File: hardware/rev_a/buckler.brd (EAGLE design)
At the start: 160 x 100 mm, 19 parts, among them J1 ARDUINO_R3_SHIELD_ICSP_NRF528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, J2 DM3AT-SF-PEJM5, U11 SI7021-A20-GM1, U12 SIP32510, U14 MPU-9250, U8 MAX44009, U9 MS5637-02BA03

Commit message: Checkpoint. Done with schematic
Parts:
- added A1: NHD-0216KZWSERIAL, headers:NHD-0216KZW
- added C1, C2, C3, C4: 0.1uF, passives:0402_CAP
- added D1: (no value), passives:SOD923
- added D2: RED, leds:LED-0603
- added D3: GREEN, leds:LED-0603
- added D4: BLUE, leds:LED-0603
- added D5: YELLOW, leds:LED-0603
- added J3: DB25_5747846, headers:DB25_5747846
- added J4, J5, J6, J7, J8, J9: 4P-2.0, headers:HW4-2.0
- added R10, R11, R2, R3, R4: 10k, passives:0402_RES
- added R5, R6, R7, R8: 1k, passives:0402_RES
- added S1, S3, S7: PTS645SM43SMTR92, switches:PTS645
- added S2: B3U-1000P, switches:B3U-1000P
- added S25, S4: TE_SSA12/SPDT, switches:TE_SSA12/SPDT
- added TP1, TP2, TP27, TP28, TP3, TP4, TP5: TEST_POINT_0.040IN, headers:TESTPOINT_0.040IN
- added U1: ADXL327, chips:LFCSP-16
- J1: value ARDUINO_R3_SHIELD_ICSP_NRF52840DK -> NRF52840DK_SHIELD; device headers:ARDUINO_R3_SHIELD_ICSP_NRF52840DK -> headers:NRF52840DK_SHIELD
- moved J1 4.02 mm to (15.2, 62.2)
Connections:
- removed net !IMU_INT: R1.1, U14.12
- removed net !LT_INT: R9.1, U8.4
- removed net N$34: U9.3
- removed net N$41: U9.2
- removed net N$50: U11.6
- removed net N$51: U8.6
- removed net N$52: U8.5
- new net !BUTTON_0: J1.P1.12, R10.1, S1.1, S1.2
- new net !BUTTON_1: J1.P1.13, R11.1, S3.1, S3.2
- new net !IMU_INTERRUPT: J1.P1.01, R1.1, TP5.TESTPOINT, U14.12
- new net !LCD_CS: A1.16, J1.P1.03
- new net !LED_0: D2.C, J1.P1.06
- new net !LED_1: D3.C, J1.P1.07
- new net !LED_2: D4.C, J1.P1.10
- new net !LED_3: D5.C, J1.P1.11
- new net !LIGHT_INTERRUPT: J1.P1.02, R9.1, TP4.TESTPOINT, U8.4
- new net ANALOG_ACCEL_X: C4.1, J1.P0.29, TP28.TESTPOINT, U1.12
- new net ANALOG_ACCEL_Y: C3.1, J1.P0.30, TP27.TESTPOINT, U1.10
- new net ANALOG_ACCEL_Z: C2.1, J1.P0.31, TP1.TESTPOINT, U1.8
- new net EXTERN_RX: J1.P0.25, J3.1, J5.2
- new net EXTERN_TX: J1.P0.24, J3.2, J5.1
- new net GROVE_A0: J1.P0.02, J6.1
- new net GROVE_A1: J1.P0.03, J6.2
- new net GROVE_A2: J1.P0.28, J7.1
- new net GROVE_D0: J1.P0.04, J8.1
- new net GROVE_D1: J1.P1.08, J8.2
- new net GROVE_D2: J1.P1.09, J9.1
- new net LCD_MISO: A1.13, J1.P0.14
- new net LCD_MOSI: A1.14, J1.P0.16
- new net LCD_SCLK: A1.12, J1.P0.12
- new net N$2: D1.P$2, J3.8, J3.9
- new net N$25: D2.A, R5.2
- new net N$3: D3.A, R6.2
- new net N$4: D4.A, R7.2
- new net N$5: D5.A, R8.2
- new net N$7: S2.1, U1.2
- new net SWITCH_0: J1.P1.14, S25.IN
- new net SWITCH_1: J1.P1.15, S4.IN
- net !SD_CS: now also J1.P1.04
- net !SD_DETECT: now also J1.P1.05
- net +3V3: now also A1.2, C1.1, J1.3.3V@0, J1.3.3V@1, J1.3.3V@2, J4.3, J5.3, J6.3, J7.3, J8.3, J9.3, R10.2, R11.2, R2.2, R3.2, R4.2, R5.1, R6.1, R7.1, R8.1, S2.2, S25.2, S4.2, U1.14, U1.15; no longer J1.3.3V, J1.IOREF
- net +5V: now also D1.P$1; no longer J1.5V_ICSP
- net GND: now also A1.1, C1.2, C2.2, C3.2, C4.2, J1.GND@3, J3.16, J3.20, J3.21, J3.24, J3.25, J3.6, J4.4, J5.4, J6.4, J7.4, J8.4, J9.4, S1.3, S1.4, S25.1, S3.3, S3.4, S4.1, S7.3, S7.4, U1.3, U1.5, U1.6, U1.7; no longer J1.GND_ICSP
- net N$1: now also J1.P0.18, R2.1, S7.1, S7.2; no longer U11.1
- net SD_MISO: now also J1.P0.13
- net SD_MOSI: now also J1.P0.15
- net SD_SCLK: now also J1.P0.11
- net SENSORS_SCL: now also J1.P0.27, J4.1, R3.1, TP3.TESTPOINT, U11.6, U8.5, U9.3
- net SENSORS_SDA: now also J1.P0.26, J4.2, R4.1, TP2.TESTPOINT, U11.1, U8.6, U9.2

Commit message: Checkpoint. 50 airwares remaining!
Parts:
- removed TP1, TP2, TP27, TP28, TP3: TEST_POINT_0.040IN, headers:TESTPOINT_0.040IN
- added TP10, TP11, TP12, TP13, TP14, TP15, TP16, TP17, TP18, TP19, TP20, TP21, TP22, TP23, TP24, TP25, TP26, TP29, TP30, TP31, TP32, TP33, TP34, TP35, TP36, TP37, TP38, TP39, TP40, TP41, TP42, TP43, TP44, TP6, TP7, TP8, TP9: TEST_POINT_0.040IN, headers:TESTPOINT_0.040IN
- moved J9 375.4 mm to (55.9, 10.2), turned to 90 degrees
- moved J8 351.2 mm to (25.4, 10.2), turned to 90 degrees
- moved J7 343.7 mm to (35.6, 10.2), turned to 90 degrees
- moved R4 337.1 mm to (54.0, 103.5), turned to 180 degrees
- moved J6 336.9 mm to (45.7, 10.2), turned to 90 degrees
- moved R3 334.9 mm to (56.5, 103.5)
- moved S7 319.3 mm to (6.35, 114.3)
- moved R2 318.5 mm to (13.3, 117.5), turned to 90 degrees
- moved S25 313.7 mm to (21.6, 30.5)
- moved S4 313.7 mm to (21.6, 21.6)
- moved J5 308.2 mm to (5.08, 10.2), turned to 90 degrees
- moved R11 303.7 mm to (14.6, 27.3)
- moved J4 300.6 mm to (15.2, 10.2), turned to 90 degrees
- moved R10 294.9 mm to (14.6, 30.5)
- moved S3 291.3 mm to (7.62, 22.9)
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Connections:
- net !BUTTON_0: now also TP36.TESTPOINT
- net !BUTTON_1: now also TP37.TESTPOINT
- net !IMU_INTERRUPT: now also TP6.TESTPOINT; no longer TP5.TESTPOINT
- net !LCD_CS: now also TP8.TESTPOINT
- net !LED_0: now also TP11.TESTPOINT
- net !LED_1: now also TP12.TESTPOINT
- net !LED_2: now also TP13.TESTPOINT
- net !LED_3: now also TP35.TESTPOINT
- net !LIGHT_INTERRUPT: now also TP7.TESTPOINT; no longer TP4.TESTPOINT
- net !SD_CS: now also TP9.TESTPOINT
- net !SD_DETECT: now also TP10.TESTPOINT
- net +3V3: now also TP4.TESTPOINT, TP40.TESTPOINT, TP5.TESTPOINT
- net +5V: now also TP41.TESTPOINT
- net ANALOG_ACCEL_X: now also TP17.TESTPOINT; no longer TP28.TESTPOINT
- net ANALOG_ACCEL_Y: now also TP18.TESTPOINT; no longer TP27.TESTPOINT
- net ANALOG_ACCEL_Z: now also TP19.TESTPOINT; no longer TP1.TESTPOINT
- net EXTERN_RX: now also TP32.TESTPOINT
- net EXTERN_TX: now also TP33.TESTPOINT
- net GND: now also TP42.TESTPOINT, TP43.TESTPOINT, TP44.TESTPOINT
- net GROVE_A0: now also TP14.TESTPOINT
- net GROVE_A1: now also TP15.TESTPOINT
- net GROVE_A2: now also TP16.TESTPOINT
- net GROVE_D0: now also TP34.TESTPOINT
- net GROVE_D1: now also TP29.TESTPOINT
- net GROVE_D2: now also TP26.TESTPOINT
- net LCD_MISO: now also TP22.TESTPOINT
- net LCD_MOSI: now also TP20.TESTPOINT
- net LCD_SCLK: now also TP24.TESTPOINT
- net SD_MISO: now also TP23.TESTPOINT
- net SD_MOSI: now also TP21.TESTPOINT
- net SD_SCLK: now also TP25.TESTPOINT
- net SENSORS_SCL: now also TP30.TESTPOINT; no longer TP3.TESTPOINT
- net SENSORS_SDA: now also TP31.TESTPOINT; no longer TP2.TESTPOINT
- net SWITCH_0: now also TP38.TESTPOINT
- net SWITCH_1: now also TP39.TESTPOINT
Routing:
- net N$1: track 0.00 -> 125.3 mm
- net EXTERN_RX: track 0.00 -> 99.0 mm, vias 0 -> 1
- net EXTERN_TX: track 0.00 -> 95.7 mm
- net GROVE_A1: track 0.00 -> 93.4 mm, vias 0 -> 1
- net GROVE_A2: track 0.00 -> 82.4 mm
- net GND: track 0.00 -> 79.2 mm, vias 0 -> 12
- net GROVE_D0: track 0.00 -> 72.0 mm
- net GROVE_D2: track 0.00 -> 67.1 mm, vias 0 -> 2
- net GROVE_A0: track 0.00 -> 36.4 mm, vias 0 -> 2
- net N$2: track 0.00 -> 35.4 mm, vias 0 -> 1
- net ANALOG_ACCEL_Y: track 0.00 -> 34.2 mm, vias 0 -> 1
- net ANALOG_ACCEL_Z: track 0.00 -> 33.5 mm, vias 0 -> 1
- net ANALOG_ACCEL_X: track 0.00 -> 33.3 mm, vias 0 -> 1
- net !BUTTON_1: track 0.00 -> 32.4 mm, vias 0 -> 2
- net GROVE_D1: track 0.00 -> 31.9 mm, vias 0 -> 1
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- added copper zone on layer 1, net +3V3
- added copper zone on layer 16, net GND
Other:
- board size 160 x 100 mm -> 63.5 x 125.7 mm

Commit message: Routing complete!!
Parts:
- added C13: 10nF, passives:0402_CAP
- added C5: 100nF, passives:0402_CAP
- moved R8 89.0 mm to (55.9, 116.2), turned to 180 degrees
- moved D3 86.0 mm to (52.7, 116.2), turned to 90 degrees
- moved D1 47.7 mm to (16.5, 81.3)
- moved R17 13.9 mm to (29.8, 95.9), turned to 0 degrees
- moved R1 13.6 mm to (27.3, 73.7), turned to 180 degrees
- moved U14 12.1 mm to (31.8, 76.2), turned to 270 degrees
- moved C18 10.6 mm to (27.3, 75.6), turned to 180 degrees
- moved R12 10.5 mm to (20.3, 101.6)
- moved C26 6.63 mm to (23.1, 103.0), turned to 0 degrees
- moved U12 5.46 mm to (26.0, 95.9), turned to 180 degrees
- moved R14 4.62 mm to (22.2, 106.7), turned to 0 degrees
- moved R16 4.49 mm to (22.2, 108.6), turned to 0 degrees
- moved R13 2.69 mm to (29.8, 99.7), turned to 180 degrees
- moved D5 2.54 mm to (6.35, 43.8)
- moved D4 2.54 mm to (8.89, 43.8)
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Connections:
- removed net !LED_3: D5.C, J1.P1.11, TP35.TESTPOINT
- net !LED_1: now also D5.C; no longer D3.C
- net +3V3: now also C13.1, C5.1
- net GND: now also C13.2, C5.2, D3.C
- net N$3: now also R8.2; no longer R6.2
- net N$5: now also R6.2; no longer R8.2
- net SD_ENABLE: now also J1.P1.11, TP35.TESTPOINT
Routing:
- net SENSORS_SCL: track 24.5 -> 142.7 mm, vias 3 -> 8
- net SENSORS_SDA: track 30.9 -> 142.4 mm, vias 0 -> 1
- net SD_MISO: track 13.4 -> 123.2 mm, vias 0 -> 3
- net SD_SCLK: track 9.83 -> 119.0 mm, vias 0 -> 3
- net SD_MOSI: track 17.0 -> 117.2 mm, vias 0 -> 2
- net !BUTTON_0: track 21.1 -> 104.0 mm, vias 0 -> 4
- net !SD_DETECT: track 5.71 -> 86.0 mm, vias 0 -> 2
- net !BUTTON_1: track 32.4 -> 111.2 mm, vias 2 -> 6
- net GROVE_A0: track 36.4 -> 113.4 mm
- net SWITCH_1: track 20.9 -> 97.0 mm, vias 0 -> 4
- net !LED_2: track 9.30 -> 85.4 mm, vias 0 -> 4
- net SWITCH_0: track 11.7 -> 87.2 mm, vias 0 -> 4
- net !SD_CS: track 5.71 -> 74.5 mm, vias 0 -> 4
- net LCD_SCLK: track 9.83 -> 70.3 mm, vias 0 -> 1
- net !LED_1: track 14.2 -> 72.7 mm, vias 0 -> 5
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
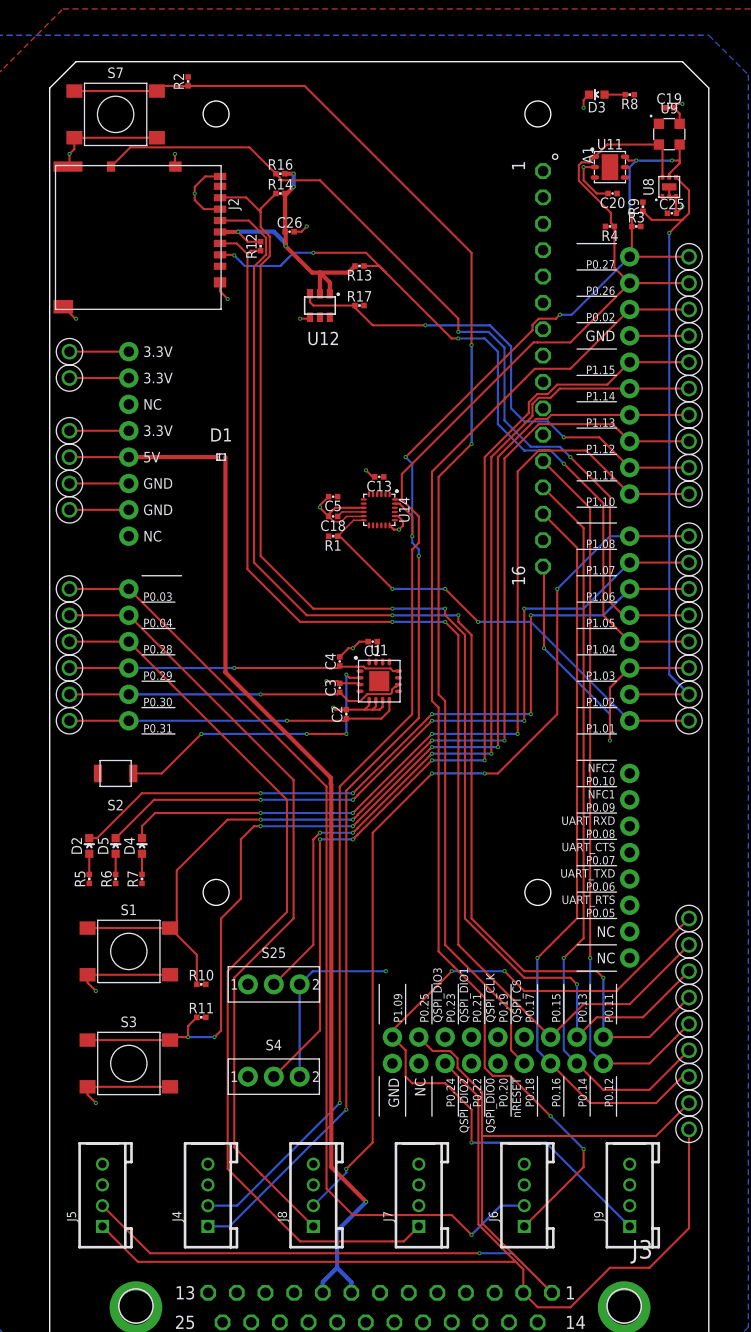
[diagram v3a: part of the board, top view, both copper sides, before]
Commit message: Renumber script, plus some manual tweaks
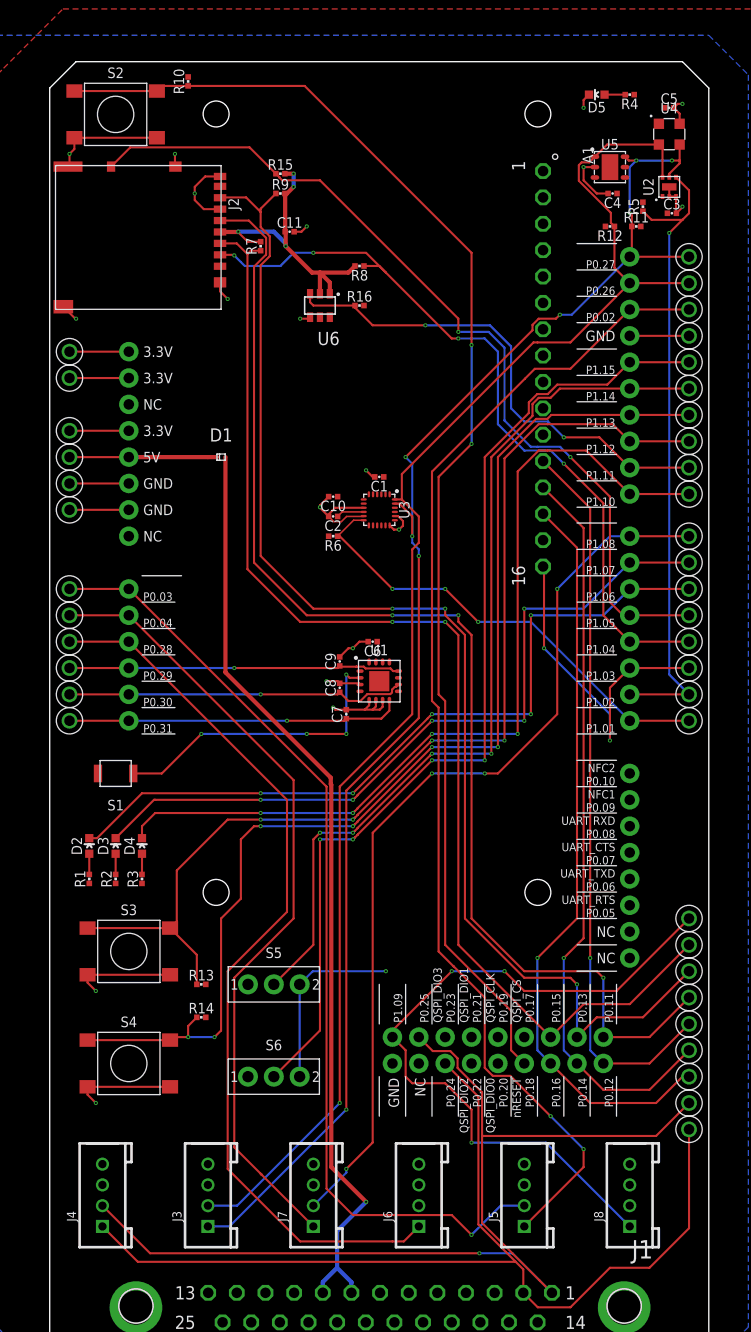
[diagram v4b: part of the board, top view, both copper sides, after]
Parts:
- removed C13: 10nF, passives:0402_CAP
- removed C18: 100nF, passives:0402_CAP
- removed C19, C20: 0.1uF, passives:0402_CAP
- removed C25: 1uF, passives:0402_CAP
- removed R17: 100k, passives:0402_RES
- removed S7: PTS645SM43SMTR92, switches:PTS645
- removed TP40, TP41, TP42, TP43, TP44: TEST_POINT_0.040IN, headers:TESTPOINT_0.040IN
- added C10, C6, C7, C8, C9: 100nF, passives:0402_CAP
- added R15: 100k, passives:0402_RES
- added S6: TE_SSA12/SPDT, switches:TE_SSA12/SPDT
- added TP1, TP2, TP27, TP28, TP3: TEST_POINT_0.040IN, headers:TESTPOINT_0.040IN
- C1: value 0.1uF -> 10nF
- C2, C3, C4: value 0.1uF -> 100nF
- D3: value GREEN -> YELLOW
- D5: value YELLOW -> GREEN
- J1: value NRF52840DK_SHIELD -> DB25_5747846; device headers:NRF52840DK_SHIELD -> headers:DB25_5747846
- J3: value DB25_5747846 -> 4P-2.0; device headers:DB25_5747846 -> headers:HW4-2.0
- J9: value 4P-2.0 -> NRF52840DK_SHIELD; device headers:HW4-2.0 -> headers:NRF52840DK_SHIELD
- R1, R2, R3, R4: value 10k -> 1k
- R5, R6, R7, R8: value 1k -> 10k
- S1: value PTS645SM43SMTR92 -> B3U-1000P; device switches:PTS645 -> switches:B3U-1000P
- S2: value B3U-1000P -> PTS645SM43SMTR92; device switches:B3U-1000P -> switches:PTS645
- S4: value TE_SSA12/SPDT -> PTS645SM43SMTR92; device switches:TE_SSA12/SPDT -> switches:PTS645
- moved J1 99.4 mm to (48.4, 0.76), turned to 180 degrees
- moved TP33 95.8 mm to (1.91, 91.4)
- moved J9 94.5 mm to (7.62, 91.4), turned to 0 degrees
- moved R10 87.0 mm to (13.3, 117.5), turned to 90 degrees
- moved R11 87.0 mm to (56.5, 103.5)
- moved D3 86.0 mm to (6.35, 43.8), turned to 0 degrees
- moved D5 86.0 mm to (52.7, 116.2), turned to 90 degrees
- moved R5 83.9 mm to (57.1, 105.4)
- moved R14 79.7 mm to (14.6, 27.3)
- moved R3 78.9 mm to (8.89, 40.6), turned to 90 degrees
- moved R2 77.2 mm to (6.35, 40.6)
- moved TP15 76.0 mm to (61.6, 21.6)
- moved TP14 71.6 mm to (1.91, 55.9)
- moved TP32 71.4 mm to (61.6, 90.4)
- moved TP24 71.4 mm to (61.6, 98.0)
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- renumbered C26 to C11, S25 to S5, U11 to U5, U12 to U6, U14 to U3, U8 to U2, U9 to U4
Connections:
- net !BUTTON_0: now also J9.P1.12, R13.1, S3.1, S3.2, TP29.TESTPOINT; no longer J1.P1.12, R10.1, S1.1, S1.2, TP36.TESTPOINT
- net !BUTTON_1: now also J9.P1.13, R14.1, S4.1, S4.2, TP30.TESTPOINT; no longer J1.P1.13, R11.1, S3.1, S3.2, TP37.TESTPOINT
- net !IMU_INTERRUPT: now also J9.P1.01, R6.1, TP1.TESTPOINT; no longer J1.P1.01, R1.1, TP6.TESTPOINT
- net !LCD_CS: now also J9.P1.03, TP3.TESTPOINT; no longer J1.P1.03, TP8.TESTPOINT
- net !LED_0: now also J9.P1.06, TP6.TESTPOINT; no longer J1.P1.06, TP11.TESTPOINT
- net !LED_1: now also D3.C, J9.P1.07, TP7.TESTPOINT; no longer D5.C, J1.P1.07, TP12.TESTPOINT
- net !LED_2: now also J9.P1.10, TP8.TESTPOINT; no longer J1.P1.10, TP13.TESTPOINT
- net !LIGHT_INTERRUPT: now also J9.P1.02, R5.1, TP2.TESTPOINT; no longer J1.P1.02, R9.1, TP7.TESTPOINT
- net !SD_CS: now also J9.P1.04, R8.1, TP4.TESTPOINT; no longer J1.P1.04, R13.1, TP9.TESTPOINT
- net !SD_DETECT: now also J9.P1.05, R15.1, TP5.TESTPOINT; no longer J1.P1.05, R16.1, TP10.TESTPOINT
- net +3V3: now also C10.1, C3.1, C4.1, C6.1, J3.3, J9.3.3V@0, J9.3.3V@1, J9.3.3V@2, R1.1, R12.2, R13.2, R14.2, R16.2, R2.1, R3.1, R4.1, R5.2, R6.2, S1.2, S6.2, TP33.TESTPOINT, TP34.TESTPOINT, TP35.TESTPOINT; no longer C13.1, C19.1, C20.1, C25.1, J1.3.3V@0, J1.3.3V@1, J1.3.3V@2, J9.3, R1.2, R17.2, R2.2, R3.2, R4.2, R5.1, R6.1, R7.1, R8.1, R9.2, S2.2, S4.2, TP4.TESTPOINT, TP40.TESTPOINT, TP5.TESTPOINT
- net +5V: now also J9.5V, TP36.TESTPOINT; no longer J1.5V, TP41.TESTPOINT
- net ANALOG_ACCEL_X: now also C9.1, J9.P0.29, TP12.TESTPOINT; no longer C4.1, J1.P0.29, TP17.TESTPOINT
- net ANALOG_ACCEL_Y: now also C8.1, J9.P0.30, TP13.TESTPOINT; no longer C3.1, J1.P0.30, TP18.TESTPOINT
- net ANALOG_ACCEL_Z: now also C7.1, J9.P0.31, TP14.TESTPOINT; no longer C2.1, J1.P0.31, TP19.TESTPOINT
- net EXTERN_RX: now also J1.1, J4.2, J9.P0.25, TP25.TESTPOINT; no longer J1.P0.25, J3.1, J5.2, TP32.TESTPOINT
- net EXTERN_TX: now also J1.2, J4.1, J9.P0.24, TP26.TESTPOINT; no longer J1.P0.24, J3.2, J5.1, TP33.TESTPOINT
- net GND: now also C10.2, C6.2, C7.2, C8.2, C9.2, D5.C, J1.16, J1.20, J1.21, J1.24, J1.25, J1.6, J3.4, J9.GND@0, J9.GND@1, J9.GND@2, J9.GND@3, S2.3, S2.4, S4.3, S4.4, S6.1, TP37.TESTPOINT, TP38.TESTPOINT, TP39.TESTPOINT; no longer C13.2, C18.2, C19.2, C20.2, C25.2, D3.C, J1.GND@0, J1.GND@1, J1.GND@2, J1.GND@3, J3.16, J3.20, J3.21, J3.24, J3.25, J3.6, J9.4, S1.3, S1.4, S4.1, S7.3, S7.4, TP42.TESTPOINT, TP43.TESTPOINT, TP44.TESTPOINT
- net GROVE_A0: now also J5.1, J9.P0.02, TP9.TESTPOINT; no longer J1.P0.02, J6.1, TP14.TESTPOINT
- net GROVE_A1: now also J5.2, J9.P0.03, TP10.TESTPOINT; no longer J1.P0.03, J6.2, TP15.TESTPOINT
- net GROVE_A2: now also J6.1, J9.P0.28, TP11.TESTPOINT; no longer J1.P0.28, J7.1, TP16.TESTPOINT
- net GROVE_D0: now also J7.1, J9.P0.04, TP27.TESTPOINT; no longer J1.P0.04, J8.1, TP34.TESTPOINT
- net GROVE_D1: now also J7.2, J9.P1.08, TP22.TESTPOINT; no longer J1.P1.08, J8.2, TP29.TESTPOINT
- net GROVE_D2: now also J8.1, J9.P1.09, TP21.TESTPOINT; no longer J1.P1.09, J9.1, TP26.TESTPOINT
- net LCD_MISO: now also J9.P0.14, TP17.TESTPOINT; no longer J1.P0.14, TP22.TESTPOINT
- net LCD_MOSI: now also J9.P0.16, TP15.TESTPOINT; no longer J1.P0.16, TP20.TESTPOINT
- net LCD_SCLK: now also J9.P0.12, TP19.TESTPOINT; no longer J1.P0.12, TP24.TESTPOINT
- net N$1: now also J9.P0.18, R10.1, S2.1, S2.2; no longer J1.P0.18, R2.1, S7.1, S7.2
- net N$18: now also R15.2, R7.2, R8.2, R9.2; no longer R12.2, R13.2, R14.2, R16.2
- net N$19: now also C2.1; no longer C18.1
- net N$2: now also J1.8, J1.9; no longer J3.8, J3.9
- net N$25: now also R1.2; no longer R5.2
- net N$3: now also D5.A, R4.2; no longer D3.A, R8.2
- net N$4: now also R3.2; no longer R7.2
- net N$5: now also D3.A, R2.2; no longer D5.A, R6.2
- net N$7: now also S1.1; no longer S2.1
- net SD_ENABLE: now also J9.P1.11, R16.1, TP28.TESTPOINT; no longer J1.P1.11, R17.1, TP35.TESTPOINT
- net SD_MISO: now also J9.P0.13, R9.1, TP18.TESTPOINT; no longer J1.P0.13, R14.1, TP23.TESTPOINT
- net SD_MOSI: now also J9.P0.15, R7.1, TP16.TESTPOINT; no longer J1.P0.15, R12.1, TP21.TESTPOINT
- net SD_SCLK: now also J9.P0.11, TP20.TESTPOINT; no longer J1.P0.11, TP25.TESTPOINT
- net SENSORS_SCL: now also J3.1, J9.P0.27, R11.1, TP23.TESTPOINT; no longer J1.P0.27, J4.1, R3.1, TP30.TESTPOINT
- net SENSORS_SDA: now also J3.2, J9.P0.26, R12.1, TP24.TESTPOINT; no longer J1.P0.26, J4.2, R4.1, TP31.TESTPOINT
- net SWITCH_0: now also J9.P1.14, TP31.TESTPOINT; no longer J1.P1.14, TP38.TESTPOINT
- net SWITCH_1: now also J9.P1.15, S6.IN, TP32.TESTPOINT; no longer J1.P1.15, S4.IN, TP39.TESTPOINT

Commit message: Checkpoint, adding part numbers
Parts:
- added TP40, TP41, TP42: TEST_POINT_0.040IN, headers:TESTPOINT_0.040IN
- D1: device passives:SOD923 -> passives:SOD323
- moved S1 1.90 mm to (6.35, 48.9)
- moved D1 1.27 mm to (15.2, 81.3)
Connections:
- net GND: now also TP40.TESTPOINT, TP41.TESTPOINT, TP42.TESTPOINT
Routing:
- net +5V: track 14.2 -> 12.2 mm
- net N$7: track 29.3 -> 30.1 mm
- net !LED_2: track 85.4 -> 84.7 mm
